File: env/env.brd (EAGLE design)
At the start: 86.3 x 107.6 mm, 96 parts, among them IC1 DG403DJD, IC2 OPA4130U, IC3 4001D, IC4 OPA2134D, IC5 OPA4130U, Q1 BC847ALT1SMD, Q2 BC857ALT1SMD, X1 2516-

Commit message: did some post fab changes to env
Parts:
- R14: value 1k -> 10k
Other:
- board text added: "On"
- board text added: "ar"
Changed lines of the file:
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@@
 <layer number="19" name="Unrouted" color="6" fill="1" visible="yes" active="yes"/>
 <layer number="20" name="Dimension" color="15" fill="1" visible="yes" active="yes"/>
-<layer number="21" name="tPlace" color="7" fill="1" visible="no" active="yes"/>
-<layer number="22" name="bPlace" color="7" fill="1" visible="no" active="yes"/>
+<layer number="21" name="tPlace" color="7" fill="1" visible="yes" active="yes"/>
+<layer number="22" name="bPlace" color="7" fill="1" visible="yes" active="yes"/>
 <layer number="23" name="tOrigins" color="15" fill="1" visible="yes" active="yes"/>
 <layer number="24" name="bOrigins" color="15" fill="1" visible="yes" active="yes"/>
@@
 <text x="64.77" y="12.7" size="1.778" layer="21" font="vector" ratio="15" rot="R270">DCV</text>
 <text x="81.28" y="11.43" size="1.778" layer="21" font="vector" ratio="15" rot="R270">OUT</text>
+<text x="34.29" y="97.79" size="1.778" layer="21" rot="R180">On</text>
+<text x="52.07" y="97.79" size="1.778" layer="21" rot="R180"> ar</text>
 </plain>
 <attributes>
@@
 <attribute name="VALUE" x="38.735" y="57.785" size="1.27" layer="21" font="vector" ratio="15" rot="R270"/>
 </element>
-<element name="R14" library="dan" package="R0603" value="1k" x="38.1" y="22.86" smashed="yes" rot="R90">
+<element name="R14" library="dan" package="R0603" value="10k" x="38.1" y="22.86" smashed="yes" rot="R90">
 <attribute name="NAME" x="36.195" y="27.305" size="1.27" layer="21" font="vector" ratio="15" rot="R270"/>
 <attribute name="VALUE" x="36.195" y="23.495" size="1.27" layer="21" font="vector" ratio="15" rot="R270"/>

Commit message: made changes to env to send out again.  need to fix bi color led.
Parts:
- added Q3, Q4: BC847ALT1SMD, dan:SOT23
- added R49, R50, R52: 10K, dan:R0603
- added R51, R53: 1K, dan:R0603
- R10: value 1k -> 500
- R12: value 10k -> 4.7k
- moved C16 7.62 mm to (19.1, 80.0), turned to 180 degrees
- moved R31 5.08 mm to (16.5, 82.5)
- moved R32 5.08 mm to (11.4, 82.5)
- moved R38 5.08 mm to (40.6, 61.0)
- moved R39 5.08 mm to (45.7, 61.0)
- moved C6 1.27 mm to (19.1, 53.3), turned to 90 degrees
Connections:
- removed net N$40 (its old number): OS.3, R38.1
- new net N$14: ADAR.3, Q4.3, R52.2
- new net N$37: OS.1, R38.1
- new net N$51: Q3.1, R10.2, R49.1
- new net N$54: IC1.15, R51.1, R7.2
- new net N$56: Q4.1, R53.1
- net +12V: now also Q3.3, R52.1
- net -12V: now also R50.2
- net ENV: now also ASHAPE.1; no longer ASHAPE.3
- net GND: now also ACVA.1, ASHAPE.3, Q4.2, R49.2; no longer ACVA.3, ASHAPE.1, IC2.3
- net N$11: now also Q3.2, R50.1, R51.2; no longer IC1.15, R10.2, R7.2
- net N$13: now also IC2.3
- net N$16: now also IC2.12; no longer IC2.13
- net N$17: now also IC2.13; no longer IC2.12
- net N$20: now also R53.2; no longer ADAR.3
- net N$28: now also R32.1; no longer R31.2
- net N$30: now also R31.2; no longer R32.1
- net N$38: now also ACVA.3; no longer ACVA.1
- net N$39: now also OS.3; no longer OS.1
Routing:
- net N$51: track 0.00 -> 21.3 mm, vias 0 -> 2
- net N$14: track 0.00 -> 18.0 mm, vias 0 -> 1
- net -12V: track 354.8 -> 371.5 mm, vias 16 -> 17
- net ENV: track 177.8 -> 193.9 mm, vias 10 -> 11
- net N$54: track 0.00 -> 14.6 mm
- net +12V: track 422.2 -> 435.7 mm, vias 25 -> 26
- net N$13: track 12.0 -> 19.1 mm, vias 2 -> 3
- net N$20: track 68.0 -> 63.2 mm
- net N$11: track 10.3 -> 5.94 mm
- net N$56: track 0.00 -> 3.81 mm
- net N$38: track 69.0 -> 72.2 mm
- net N$45: track 78.2 -> 75.5 mm
- net N$40 (its old number): track 2.33 -> 0.00 mm
- net N$37: track 0.00 -> 2.33 mm
- net N$55: track 10.0 -> 7.97 mm, vias 1 -> 0
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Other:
- board text added: "3904"
- board text added: "3906"
- board text added: "AR"
- board text removed: "ar"

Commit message: got the 2nd set of gerbers for env ready to send out
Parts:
- removed D1: (no value), dan:DUOLED5MM
- added LED3: (no value), dan:LED5MM
- R9: value 10k -> 4.7k
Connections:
- removed net N$52: D1.AG, D1.AR, R48.1
- new net N$57: LED3.K, R48.1
- net N$36: now also LED3.A; no longer D1.K
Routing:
- net N$52: track 11.6 -> 0.00 mm
- net N$57: track 0.00 -> 4.23 mm
- net N$36: track 147.7 -> 148.2 mm
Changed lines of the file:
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@@
 <attribute name="VALUE" x="33.655" y="47.625" size="1.27" layer="21" font="vector" ratio="15" rot="R270"/>
 </element>
-<element name="R9" library="dan" package="R0603" value="10k" x="35.56" y="50.8" smashed="yes">
-<attribute name="NAME" x="37.465" y="50.165" size="1.27" layer="21" font="vector" ratio="15" rot="R270"/>
+<element name="R9" library="dan" package="R0603" value="4.7k" x="35.56" y="50.8" smashed="yes">
+<attribute name="NAME" x="34.925" y="51.435" size="1.27" layer="21" font="vector" ratio="15"/>
 <attribute name="VALUE" x="33.655" y="55.245" size="1.27" layer="21" font="vector" ratio="15" rot="R270"/>
 </element>
@@
 <attribute name="VALUE" x="81.915" y="23.495" size="1.27" layer="21" font="vector" ratio="15" rot="R270"/>
 </element>
-<element name="D1" library="dan" package="DUOLED5MM" value="" x="43.18" y="91.44" smashed="yes" rot="R90">
-<attribute name="NAME" x="46.1264" y="94.996" size="1.27" layer="21" font="vector" ratio="15" rot="R270"/>
-<attribute name="VALUE" x="45.6184" y="94.2594" size="1.27" layer="27" ratio="10" rot="R90"/>
-</element>
 <element name="LED1" library="dan" package="LED5MM" value="" x="74.93" y="25.4" smashed="yes" rot="R90">
 <attribute name="NAME" x="70.3834" y="27.305" size="1.27" layer="21" font="vector" ratio="15" rot="R270"/>
@@
 <attribute name="NAME" x="59.055" y="84.455" size="1.27" layer="21" font="vector" ratio="15" rot="R270"/>
 <attribute name="VALUE" x="56.515" y="84.455" size="1.27" layer="21" font="vector" ratio="15" rot="R270"/>
+</element>
+<element name="LED3" library="dan" package="LED5MM" value="" x="43.18" y="91.44" smashed="yes" rot="R270">
+<attribute name="NAME" x="46.2534" y="89.535" size="1.27" layer="21" font="vector" ratio="14" rot="R270"/>
+<attribute name="VALUE" x="41.3766" y="88.2396" size="1.27" layer="27" ratio="10" rot="R270"/>
 </element>
 </elements>
@@
 <via x="58.42" y="96.52" extent="1-16" drill="0.7"/>
 <via x="39.37" y="93.98" extent="1-16" drill="0.7"/>
-<via x="46.99" y="86.36" extent="1-16" drill="0.7"/>
-<via x="46.99" y="83.82" extent="1-16" drill="0.7"/>
+<via x="46.99" y="95.25" extent="1-16" drill="0.7"/>
+<via x="45.72" y="86.36" extent="1-16" drill="0.7"/>
 <via x="24.13" y="97.79" extent="1-16" drill="0.7"/>
 <via x="29.21" y="95.25" extent="1-16" drill="0.7"/>
@@
 <wire x1="26.67" y1="93.81" x2="26.67" y2="96.52" width="0.6096" layer="1"/>
 <via x="26.67" y="96.52" extent="1-16" drill="0.7"/>
-<wire x1="59.69" y1="93.56" x2="57.57" y2="93.56" width="0.4064" layer="1"/>
-<wire x1="57.57" y1="93.56" x2="57.15" y2="93.98" width="0.4064" layer="1"/>
+<wire x1="59.69" y1="93.56" x2="57.57" y2="93.56" width="0.6096" layer="1"/>
+<wire x1="57.57" y1="93.56" x2="57.15" y2="93.98" width="0.6096" layer="1"/>
 <wire x1="17.78" y1="55.88" x2="17.78" y2="52.07" width="0.6096" layer="1"/>
 <wire x1="17.78" y1="52.07" x2="18.63" y2="52.07" width="0.6096" layer="1"/>
@@
 <wire x1="62.23" y1="55.88" x2="62.23" y2="54.0766" width="0.4064" layer="1"/>
 <wire x1="62.23" y1="54.0766" x2="62.7634" y2="53.34" width="0.4064" layer="1"/>
-<contactref element="D1" pad="K"/>
-<wire x1="43.18" y1="91.44" x2="64.77" y2="91.44" width="0.4064" layer="16"/>
 <wire x1="64.77" y1="91.44" x2="66.04" y2="90.17" width="0.4064" layer="16"/>
-<wire x1="74.93" y1="90.17" x2="78.74" y2="90.17" width="0.4064" layer="16"/>
 <wire x1="66.04" y1="90.17" x2="69.85" y2="90.17" width="0.4064" layer="16"/>
 <wire x1="69.85" y1="90.17" x2="71.12" y2="91.44" width="0.4064" layer="16"/>
 <wire x1="71.12" y1="91.44" x2="73.66" y2="91.44" width="0.4064" layer="16"/>
 <wire x1="73.66" y1="91.44" x2="74.93" y2="90.17" width="0.4064" layer="16"/>
-<wire x1="78.74" y1="90.17" x2="83.82" y2="90.17" width="0.4064" layer="16"/>
+<wire x1="74.93" y1="90.17" x2="83.82" y2="90.17" width="0.4064" layer="16"/>
 <via x="83.82" y="90.17" extent="1-16" drill="0.7"/>
 <wire x1="83.82" y1="90.17" x2="83.82" y2="55.88" width="0.4064" layer="1"/>
+<contactref element="LED3" pad="A"/>
+<wire x1="43.18" y1="92.71" x2="46.99" y2="92.71" width="0.4064" layer="16"/>
+<wire x1="46.99" y1="92.71" x2="48.26" y2="91.44" width="0.4064" layer="16"/>
+<wire x1="48.26" y1="91.44" x2="64.77" y2="91.44" width="0.4064" layer="16"/>
 </signal>
 <signal name="N$41">
@@
 <wire x1="13.97" y1="60.31" x2="13.97" y2="49.53" width="0.4064" layer="1"/>
 </signal>
-<signal name="N$52">
-<contactref element="D1" pad="AG"/>
-<contactref element="D1" pad="AR"/>
-<contactref element="R48" pad="1"/>
-<wire x1="43.18" y1="85.94" x2="43.18" y2="88.9" width="0.4064" layer="1"/>
-<wire x1="43.18" y1="93.98" x2="41.91" y2="93.98" width="0.4064" layer="1"/>
-<wire x1="41.91" y1="93.98" x2="40.64" y2="92.71" width="0.4064" layer="1"/>
-<wire x1="40.64" y1="92.71" x2="40.64" y2="90.17" width="0.4064" layer="1"/>
-<wire x1="40.64" y1="90.17" x2="41.91" y2="88.9" width="0.4064" layer="1"/>
-<wire x1="41.91" y1="88.9" x2="43.18" y2="88.9" width="0.4064" layer="1"/>
-</signal>
 <signal name="N$53">
 <contactref element="R47" pad="2"/>
@@
 <wire x1="16.47" y1="83.44" x2="16.51" y2="83.4" width="0.4064" layer="1"/>
 </signal>
+<signal name="N$57">
+<contactref element="R48" pad="1"/>
+<contactref element="LED3" pad="K"/>
+<wire x1="43.18" y1="85.94" x2="43.18" y2="90.17" width="0.4064" layer="1"/>
+</signal>
 </signals>

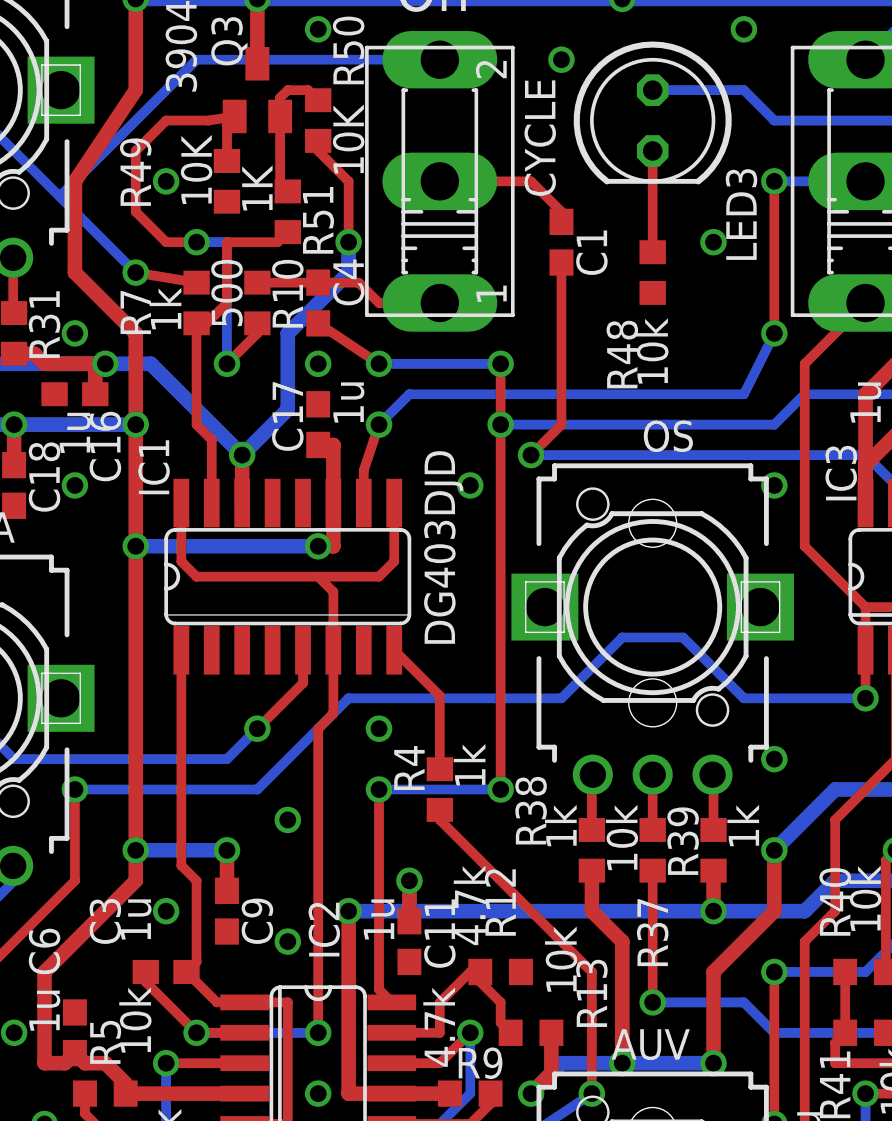
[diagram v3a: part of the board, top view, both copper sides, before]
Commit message: fixed the logic supply for the switch in the env
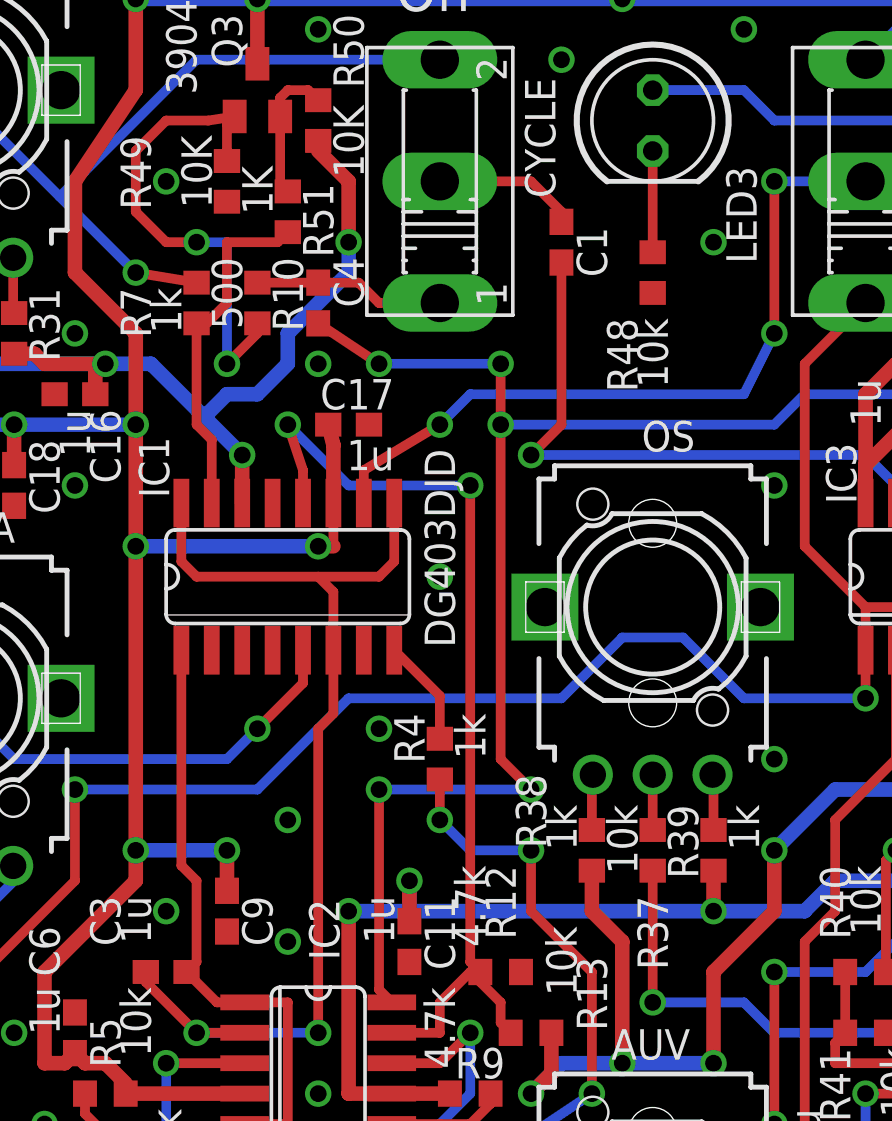
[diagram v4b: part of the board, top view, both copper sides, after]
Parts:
- moved C17 1.27 mm to (30.5, 78.7), turned to 0 degrees
- moved R4 1.27 mm to (34.3, 64.8)
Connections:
- net N$17: now also IC1.12
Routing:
- net N$17: track 8.56 -> 41.1 mm, vias 0 -> 2
- net ID: track 50.2 -> 53.0 mm, vias 4 -> 6
- net N$20: track 63.2 -> 65.0 mm
- net N$6: track 5.76 -> 4.49 mm
- net N$18: track 32.1 -> 31.3 mm
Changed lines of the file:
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@@
 <attribute name="VALUE" x="46.355" y="62.865" size="1.27" layer="21" font="vector" ratio="15" rot="R270"/>
 </element>
-<element name="R4" library="dan" package="R0603" value="1k" x="34.29" y="63.5" smashed="yes" rot="R90">
-<attribute name="NAME" x="32.385" y="65.405" size="1.27" layer="21" font="vector" ratio="15" rot="R270"/>
-<attribute name="VALUE" x="34.925" y="65.405" size="1.27" layer="21" font="vector" ratio="15" rot="R270"/>
+<element name="R4" library="dan" package="R0603" value="1k" x="34.29" y="64.77" smashed="yes" rot="R90">
+<attribute name="NAME" x="32.385" y="66.675" size="1.27" layer="21" font="vector" ratio="15" rot="R270"/>
+<attribute name="VALUE" x="34.925" y="66.675" size="1.27" layer="21" font="vector" ratio="15" rot="R270"/>
 </element>
 <element name="R40" library="dan" package="R0603" value="10k" x="52.07" y="55.88" smashed="yes">
@@
 <attribute name="VALUE" x="18.415" y="79.375" size="1.27" layer="21" font="vector" ratio="15" rot="R270"/>
 </element>
-<element name="C17" library="dan" package="C0603" value="1u" x="29.21" y="78.74" smashed="yes" rot="R90">
-<attribute name="NAME" x="27.305" y="80.645" size="1.27" layer="21" font="vector" ratio="15" rot="R270"/>
-<attribute name="VALUE" x="29.845" y="80.645" size="1.27" layer="21" font="vector" ratio="15" rot="R270"/>
+<element name="C17" library="dan" package="C0603" value="1u" x="30.48" y="78.74" smashed="yes">
+<attribute name="NAME" x="32.385" y="80.645" size="1.27" layer="21" font="vector" ratio="15" rot="R180"/>
+<attribute name="VALUE" x="32.385" y="78.105" size="1.27" layer="21" font="vector" ratio="15" rot="R180"/>
 </element>
 <element name="C18" library="dan" package="C0603" value="1u" x="16.51" y="76.2" smashed="yes" rot="R270">
@@
 <via x="19.05" y="82.55" extent="1-16" drill="0.7"/>
 <via x="19.05" y="76.2" extent="1-16" drill="0.7"/>
-<via x="35.56" y="76.2" extent="1-16" drill="0.7"/>
+<via x="34.29" y="72.39" extent="1-16" drill="0.7"/>
 <via x="48.26" y="38.1" extent="1-16" drill="0.7"/>
 <via x="55.88" y="34.29" extent="1-16" drill="0.7"/>
@@
 <contactref element="R4" pad="2"/>
 <contactref element="IC1" pad="8"/>
-<wire x1="34.29" y1="64.35" x2="34.29" y2="67.4116" width="0.4064" layer="1"/>
+<wire x1="34.29" y1="65.62" x2="34.29" y2="67.4116" width="0.4064" layer="1"/>
 <wire x1="34.29" y1="67.4116" x2="32.385" y2="69.3166" width="0.4064" layer="1"/>
 </signal>
@@
 <via x="40.64" y="50.8" extent="1-16" drill="0.7"/>
 <wire x1="40.64" y1="50.8" x2="40.64" y2="55.88" width="0.4064" layer="1"/>
-<wire x1="40.64" y1="55.88" x2="34.29" y2="62.23" width="0.4064" layer="1"/>
-<wire x1="34.29" y1="62.23" x2="34.29" y2="62.65" width="0.4064" layer="1"/>
 <wire x1="36.83" y1="31.75" x2="46.99" y2="31.75" width="0.4064" layer="16"/>
 <wire x1="46.99" y1="31.75" x2="48.26" y2="33.02" width="0.4064" layer="16"/>
+<wire x1="40.64" y1="55.88" x2="38.1" y2="58.42" width="0.4064" layer="1"/>
+<wire x1="38.1" y1="58.42" x2="38.1" y2="60.96" width="0.4064" layer="1"/>
+<via x="38.1" y="60.96" extent="1-16" drill="0.7"/>
+<via x="34.29" y="62.23" extent="1-16" drill="0.7"/>
+<wire x1="34.29" y1="62.23" x2="34.29" y2="63.92" width="0.4064" layer="1"/>
+<wire x1="38.1" y1="60.96" x2="35.56" y2="60.96" width="0.4064" layer="16"/>
+<wire x1="35.56" y1="60.96" x2="34.29" y2="62.23" width="0.4064" layer="16"/>
 </signal>
 <signal name="ENV">
@@
 <via x="21.59" y="73.66" extent="1-16" drill="0.7"/>
 <wire x1="29.21" y1="73.66" x2="29.845" y2="73.66" width="0.6096" layer="1"/>
-<wire x1="29.845" y1="73.66" x2="29.845" y2="75.4634" width="0.6096" layer="1"/>
-<wire x1="29.21" y1="77.89" x2="29.845" y2="77.89" width="0.6096" layer="1"/>
+<wire x1="29.845" y1="73.66" x2="29.845" y2="75.4634" width="0.4064" layer="1"/>
+<wire x1="29.63" y1="78.74" x2="29.845" y2="77.89" width="0.6096" layer="1"/>
 <wire x1="29.845" y1="77.89" x2="29.845" y2="75.4634" width="0.6096" layer="1"/>
 <wire x1="52.07" y1="75.4634" x2="52.07" y2="77.05" width="0.6096" layer="1"/>
@@
 <via x="26.035" y="77.47" extent="1-16" drill="0.7"/>
 <wire x1="20.32" y1="81.28" x2="22.225" y2="81.28" width="0.6096" layer="16"/>
-<wire x1="22.225" y1="81.28" x2="26.035" y2="77.47" width="0.6096" layer="16"/>
+<wire x1="22.225" y1="81.28" x2="24.4475" y2="79.0575" width="0.6096" layer="16"/>
 <contactref element="C19" pad="1"/>
+<wire x1="24.4475" y1="79.0575" x2="26.035" y2="77.47" width="0.6096" layer="16"/>
 <wire x1="8.04" y1="77.47" x2="8.04" y2="78.32" width="0.6096" layer="1"/>
 <wire x1="8.04" y1="78.32" x2="6.35" y2="80.01" width="0.6096" layer="1"/>
@@
 <contactref element="R50" pad="2"/>
 <wire x1="29.21" y1="90.59" x2="29.21" y2="90.17" width="0.4064" layer="1"/>
-<wire x1="29.21" y1="90.17" x2="30.48" y2="88.9" width="0.4064" layer="1"/>
-<wire x1="30.48" y1="88.9" x2="30.48" y2="86.36" width="0.4064" layer="1"/>
+<wire x1="29.21" y1="90.17" x2="30.48" y2="88.9" width="0.6096" layer="1"/>
+<wire x1="30.48" y1="88.9" x2="30.48" y2="86.36" width="0.6096" layer="1"/>
 <via x="30.48" y="86.36" extent="1-16" drill="0.7"/>
 <wire x1="30.48" y1="86.36" x2="30.48" y2="85.09" width="0.6096" layer="16"/>
 <wire x1="30.48" y1="85.09" x2="27.94" y2="82.55" width="0.6096" layer="16"/>
-<wire x1="27.94" y1="82.55" x2="27.94" y2="79.375" width="0.6096" layer="16"/>
-<wire x1="27.94" y1="79.375" x2="26.035" y2="77.47" width="0.6096" layer="16"/>
 <wire x1="19.9" y1="80.01" x2="19.9" y2="80.86" width="0.6096" layer="1"/>
 <wire x1="19.9" y1="80.86" x2="20.32" y2="81.28" width="0.6096" layer="1"/>
@@
 <wire x1="17.36" y1="81.7" x2="17.78" y2="81.28" width="0.6096" layer="1"/>
 <wire x1="17.78" y1="81.28" x2="20.32" y2="81.28" width="0.6096" layer="1"/>
+<wire x1="27.94" y1="82.55" x2="27.94" y2="81.28" width="0.6096" layer="16"/>
+<wire x1="27.94" y1="81.28" x2="26.67" y2="80.01" width="0.6096" layer="16"/>
+<wire x1="26.67" y1="80.01" x2="25.4" y2="80.01" width="0.6096" layer="16"/>
+<wire x1="25.4" y1="80.01" x2="24.4475" y2="79.0575" width="0.6096" layer="16"/>
 </signal>
 <signal name="N$13">
@@
 <wire x1="34.29" y1="54.61" x2="35.56" y2="55.88" width="0.4064" layer="1"/>
 <wire x1="35.56" y1="55.88" x2="35.98" y2="55.88" width="0.4064" layer="1"/>
+<contactref element="IC1" pad="12"/>
+<wire x1="28.575" y1="75.4634" x2="28.575" y2="76.835" width="0.4064" layer="1"/>
+<wire x1="28.575" y1="76.835" x2="27.94" y2="78.74" width="0.4064" layer="1"/>
+<via x="27.94" y="78.74" extent="1-16" drill="0.7"/>
+<via x="35.56" y="76.2" extent="1-16" drill="0.7"/>
+<wire x1="35.56" y1="76.2" x2="35.56" y2="56.3" width="0.4064" layer="1"/>
+<wire x1="35.56" y1="56.3" x2="35.98" y2="55.88" width="0.4064" layer="1"/>
+<wire x1="35.56" y1="76.2" x2="30.48" y2="76.2" width="0.4064" layer="16"/>
+<wire x1="30.48" y1="76.2" x2="27.94" y2="78.74" width="0.4064" layer="16"/>
 </signal>
 <signal name="N$19">
@@
 <contactref element="IC1" pad="10"/>
 <wire x1="31.115" y1="75.4634" x2="31.115" y2="76.835" width="0.4064" layer="1"/>
-<wire x1="31.115" y1="76.835" x2="31.75" y2="78.74" width="0.4064" layer="1"/>
-<via x="31.75" y="78.74" extent="1-16" drill="0.7"/>
+<wire x1="31.115" y1="76.835" x2="34.29" y2="78.74" width="0.4064" layer="1"/>
+<via x="34.29" y="78.74" extent="1-16" drill="0.7"/>
 <via x="48.26" y="82.55" extent="1-16" drill="0.7"/>
 <wire x1="48.26" y1="82.55" x2="48.26" y2="88.9" width="0.4064" layer="1"/>
 <via x="48.26" y="88.9" extent="1-16" drill="0.7"/>
 <wire x1="48.26" y1="88.9" x2="52.07" y2="88.9" width="0.4064" layer="16"/>
-<wire x1="31.75" y1="78.74" x2="33.02" y2="80.01" width="0.4064" layer="16"/>
-<wire x1="33.02" y1="80.01" x2="46.99" y2="80.01" width="0.4064" layer="16"/>
+<wire x1="34.29" y1="78.74" x2="35.56" y2="80.01" width="0.4064" layer="16"/>
+<wire x1="35.56" y1="80.01" x2="46.99" y2="80.01" width="0.4064" layer="16"/>
 <wire x1="46.99" y1="80.01" x2="48.26" y2="82.55" width="0.4064" layer="16"/>
 </signal>
@@
 <wire x1="31.75" y1="81.28" x2="36.83" y2="81.28" width="0.4064" layer="16"/>
 <via x="31.75" y="63.5" extent="1-16" drill="0.7"/>
-<wire x1="31.75" y1="63.5" x2="36.83" y2="63.5" width="0.4064" layer="16"/>
-<via x="36.83" y="63.5" extent="1-16" drill="0.7"/>
-<wire x1="36.83" y1="63.5" x2="36.83" y2="78.74" width="0.4064" layer="1"/>
+<wire x1="31.75" y1="63.5" x2="38.1" y2="63.5" width="0.4064" layer="16"/>
+<via x="38.1" y="63.5" extent="1-16" drill="0.7"/>
 <via x="36.83" y="81.28" extent="1-16" drill="0.7"/>
 <wire x1="31.75" y1="63.5" x2="31.75" y2="55.1434" width="0.4064" layer="1"/>
@@
 <wire x1="36.83" y1="78.74" x2="36.83" y2="81.28" width="0.4064" layer="1"/>
 <wire x1="31.75" y1="55.1434" x2="32.2834" y2="54.61" width="0.4064" layer="1"/>
+<wire x1="36.83" y1="78.74" x2="36.83" y2="64.77" width="0.4064" layer="1"/>
+<wire x1="36.83" y1="64.77" x2="38.1" y2="63.5" width="0.4064" layer="1"/>
 </signal>
 <signal name="N$15">
